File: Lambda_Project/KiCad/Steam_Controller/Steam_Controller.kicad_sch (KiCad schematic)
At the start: 208 parts, among them J1 MICROQTJ, P1 Conn_ARM_SWD_TagConnect_TC2030, P2 Conn_ARM_SWD_TagConnect_TC2030, P3 781271220, P4 781271220, Q10 DMN2300U-7, Q11 DMN2300U-7, Q12 DMP2035U-7, Q2 DMP2035U-7, Q3 MMBT3906, Q4 DMP2035U-7, Q5 DMP2035U-7, Q6 FDV304P, Q8 FDV304P, U1 LPC11U37FBD64/501,, U10 DMN63D8LDW-7, U2 TPD4E1U06DBVR - NG4P USB, U3 TPS61029DRCR, U4 TLV70230DBVT, U5 NRF51822-QFAB-T, U6 MPU6500, U7 A1304ELHLT-T, U8 A1304ELHLT-T, U9 DMN63D8LDW-7, X1 ABM8-12.000MHZ-B2-T, X2 NX2520SA-16MHZ-STD-CSW-5

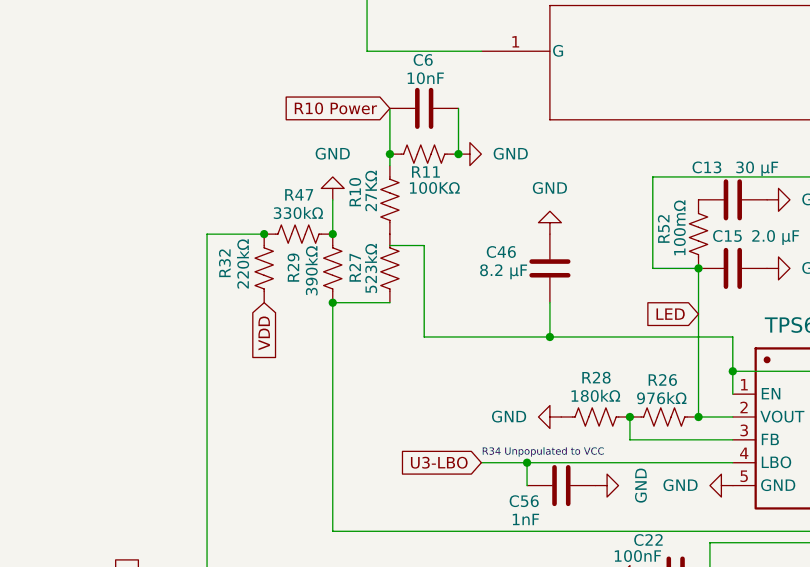
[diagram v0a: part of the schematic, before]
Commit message: Connect trigger hall effects to power
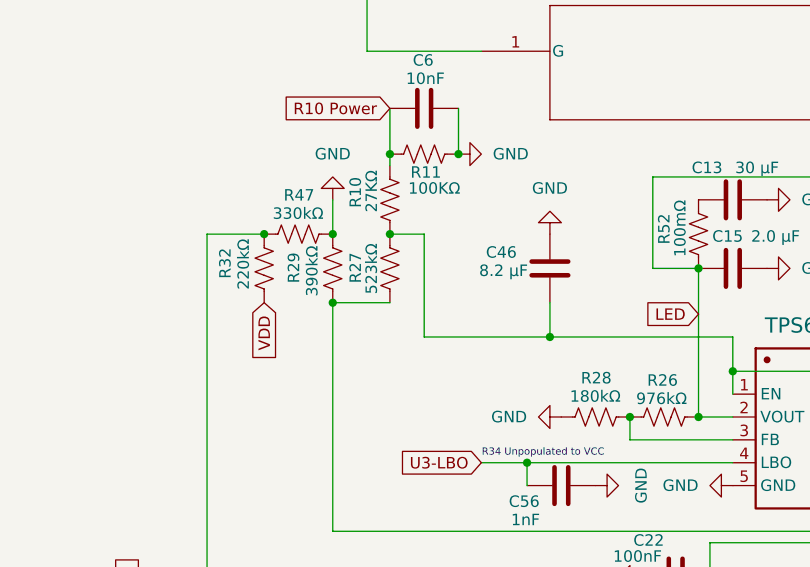
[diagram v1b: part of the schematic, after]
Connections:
- net D3-K: now also R10.2, R27.1
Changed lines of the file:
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@@
+	)
+	(junction
+		(at 203.2 309.88)
+		(diameter 0)
+		(color 0 0 0 0)
 	)
 	(junction
@@
 	(wire
 		(pts
-			(xy 203.2 311.15) (xy 207.01 311.15)
+			(xy 203.2 309.88) (xy 207.01 309.88)
 		)
 		(stroke
@@
 	(wire
 		(pts
-			(xy 207.01 311.15) (xy 207.01 321.31)
-		)
-		(stroke
+			(xy 207.01 309.88) (xy 207.01 321.31)
+		)
+		(stroke
